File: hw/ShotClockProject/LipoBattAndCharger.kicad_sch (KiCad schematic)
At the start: 28 parts, among them IC1 TP4056-42-ESOP8_Rearanged, J3 SM03B-SRSS-TB(LF)(SN)(P), J4 Conn_01x02_Pin, J5 Conn_01x03_Pin, Q1 Q_PMOS_SGD, Q2 Q_NPN_BCE, Q3 Q_NPN_BCE

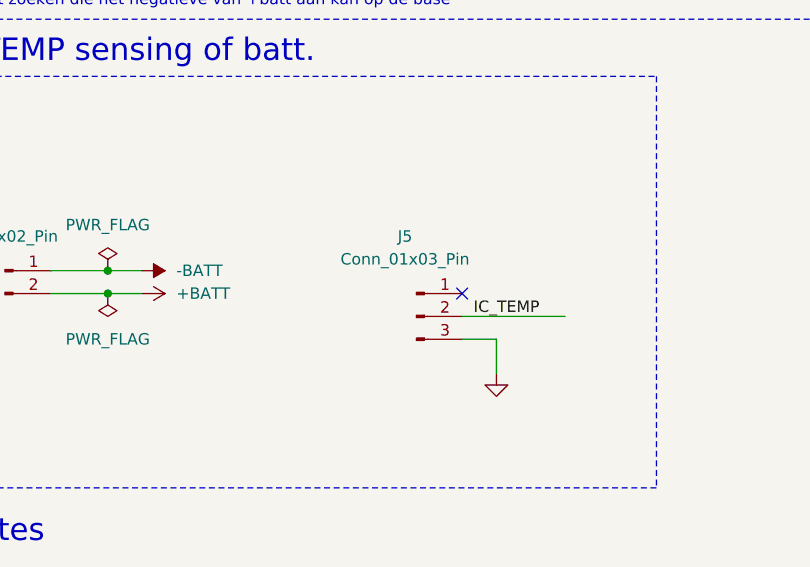
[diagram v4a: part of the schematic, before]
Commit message: Finished mainboard routing
Reconfigered pins to make routing easier/cleaner
Placed copper fills as much as possible to create an even plating index
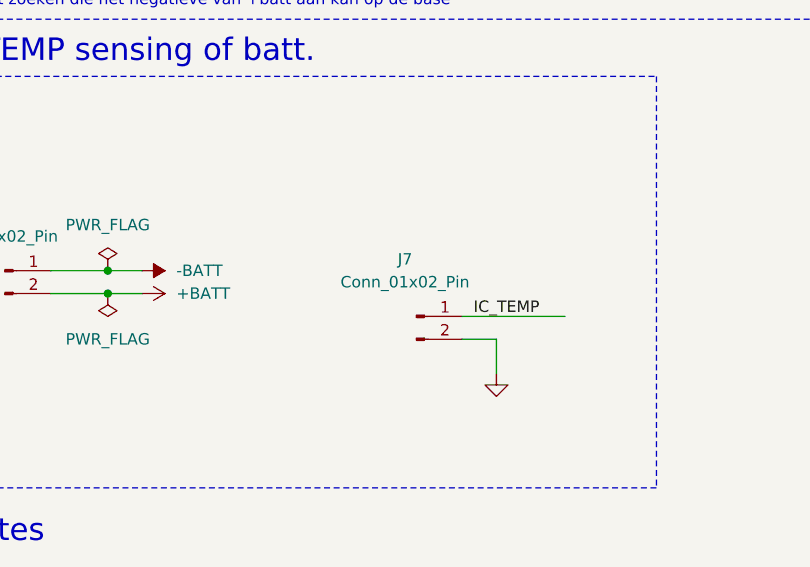
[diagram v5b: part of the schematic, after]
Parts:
- removed J5: Conn_01x03_Pin, Connector_PinHeader_2.54mm:PinHeader_1x03_P2.54mm_Horizontal, symbol Connector:Conn_01x03_Pin
- added J7: Conn_01x02_Pin, Connector_PinHeader_2.54mm:PinHeader_1x02_P2.54mm_Horizontal, symbol Connector:Conn_01x02_Pin
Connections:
- net GND: now also J7.2 (Pin_2)
- net IC_TEMP: now also J7.1 (Pin_1)
- no-connect marks 1 -> 0
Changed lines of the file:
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@@
   (junction (at 50.8 39.37) (diameter 0) (color 0 0 0 0)
   )
+  (junction (at 121.92 55.88) (diameter 0) (color 0 0 0 0)
+  )
+  (junction (at 177.8 49.53) (diameter 0) (color 0 0 0 0)
+  )
+  (junction (at 120.65 113.03) (diameter 0) (color 0 0 0 0)
+  )
+  (junction (at 152.4 67.31) (diameter 0) (color 0 0 0 0)
+  )
   (junction (at 168.91 49.53) (diameter 0) (color 0 0 0 0)
   )
-  (junction (at 121.92 55.88) (diameter 0) (color 0 0 0 0)
-  )
-  (junction (at 177.8 49.53) (diameter 0) (color 0 0 0 0)
-  )
-  (junction (at 120.65 113.03) (diameter 0) (color 0 0 0 0)
-  )
-  (junction (at 152.4 67.31) (diameter 0) (color 0 0 0 0)
-  )
   (junction (at 121.92 69.85) (diameter 0) (color 0 0 0 0)
   )
@@
   (junction (at 233.68 55.88) (diameter 0) (color 0 0 0 0)
   )
-  (no_connect (at 160.02 115.57))
   (wire (pts (xy 66.04 109.22) (xy 66.04 111.76))
     (stroke (width 0) (type default))
@@
     (stroke (width 0) (type default))
   )
+  (wire (pts (xy 152.4 58.42) (xy 152.4 62.23))
+    (stroke (width 0) (type default))
+  )
+  (wire (pts (xy 59.69 39.37) (xy 50.8 39.37))
+    (stroke (width 0) (type default))
+  )
+  (wire (pts (xy 29.21 101.6) (xy 24.765 101.6))
+    (stroke (width 0) (type default))
+  )
+  (wire (pts (xy 179.07 67.31) (xy 177.8 67.31))
+    (stroke (width 0) (type default))
+  )
+  (wire (pts (xy 114.3 113.03) (xy 120.65 113.03))
+    (stroke (width 0) (type default))
+  )
+  (wire (pts (xy 177.8 49.53) (xy 181.61 49.53))
+    (stroke (width 0) (type default))
+  )
+  (wire (pts (xy 41.91 46.99) (xy 41.91 48.26))
+    (stroke (width 0) (type default))
+  )
+  (wire (pts (xy 120.65 113.03) (xy 124.46 113.03))
+    (stroke (width 0) (type default))
+  )
+  (wire (pts (xy 160.02 120.65) (xy 163.83 120.65))
+    (stroke (width 0) (type default))
+  )
+  (wire (pts (xy 233.68 55.88) (xy 233.68 58.42))
+    (stroke (width 0) (type default))
+  )
+  (wire (pts (xy 121.92 55.88) (xy 121.92 57.15))
+    (stroke (width 0) (type default))
+  )
   (wire (pts (xy 135.89 49.53) (xy 168.91 49.53))
-    (stroke (width 0) (type default))
-  )
-  (wire (pts (xy 152.4 58.42) (xy 152.4 62.23))
-    (stroke (width 0) (type default))
-  )
-  (wire (pts (xy 59.69 39.37) (xy 50.8 39.37))
-    (stroke (width 0) (type default))
-  )
-  (wire (pts (xy 29.21 101.6) (xy 24.765 101.6))
-    (stroke (width 0) (type default))
-  )
-  (wire (pts (xy 179.07 67.31) (xy 177.8 67.31))
-    (stroke (width 0) (type default))
-  )
-  (wire (pts (xy 114.3 113.03) (xy 120.65 113.03))
-    (stroke (width 0) (type default))
-  )
-  (wire (pts (xy 177.8 49.53) (xy 181.61 49.53))
-    (stroke (width 0) (type default))
-  )
-  (wire (pts (xy 41.91 46.99) (xy 41.91 48.26))
-    (stroke (width 0) (type default))
-  )
-  (wire (pts (xy 120.65 113.03) (xy 124.46 113.03))
-    (stroke (width 0) (type default))
-  )
-  (wire (pts (xy 160.02 120.65) (xy 163.83 120.65))
-    (stroke (width 0) (type default))
-  )
-  (wire (pts (xy 233.68 55.88) (xy 233.68 58.42))
-    (stroke (width 0) (type default))
-  )
-  (wire (pts (xy 121.92 55.88) (xy 121.92 57.15))
     (stroke (width 0) (type default))
   )
@@
     (effects (font (size 1.27 1.27)) (justify left))
   )
-  (symbol (lib_id "Connector:Conn_01x03_Pin") (at 154.94 118.11 0) (unit 1)
-    (in_bom yes) (on_board yes) (dnp no)
-    (property "Reference" "J5" (at 153.67 109.22 0)
-      (effects (font (size 1.27 1.27)))
-    )
-    (property "Value" "Conn_01x03_Pin" (at 153.67 111.76 0)
-      (effects (font (size 1.27 1.27)))
-    )
-    (property "Footprint" "Connector_PinHeader_2.54mm:PinHeader_1x03_P2.54mm_Horizontal" (at 154.94 118.11 0)
-      (effects (font (size 1.27 1.27)) hide)
-    )
-    (property "Datasheet" "~" (at 154.94 118.11 0)
-      (effects (font (size 1.27 1.27)) hide)
-    )
-    (property "LCSC Part #" "C92159" (at 154.94 118.11 0)
-      (effects (font (size 1.27 1.27)) hide)
-    )
-    (property "LCSC Part" "C92159" (at 154.94 118.11 0)
-      (effects (font (size 1.27 1.27)) hide)
-    )
-    (pin "1")
-    (pin "2")
-    (pin "3")
-    (instances
-      (project "ShotClockProject"
-        (path "/5fd859aa-754d-49c2-9762-3f7ebe3bb64c/d287d155-1951-4d4f-8d6c-570f03bc79f5"
-          (reference "J5") (unit 1)
-        )
-      )
-    )
-  )
   (symbol (lib_id "Device:Q_NPN_BCE") (at 166.37 67.31 0) (unit 1)
     (in_bom yes) (on_board yes) (dnp no)
@@
         )
       )
+    )
+  )
+  (symbol (lib_id "Connector:Conn_01x02_Pin") (at 154.94 118.11 0) (unit 1)
+    (in_bom yes) (on_board yes) (dnp no)
+    (property "Reference" "J7" (at 153.67 111.76 0)
+      (effects (font (size 1.27 1.27)))
+    )
+    (property "Value" "Conn_01x02_Pin" (at 153.67 114.3 0)
+      (effects (font (size 1.27 1.27)))
+    )
+    (property "Footprint" "Connector_PinHeader_2.54mm:PinHeader_1x02_P2.54mm_Horizontal" (at 154.94 118.11 0)
+      (effects (font (size 1.27 1.27)) hide)
+    )
+    (property "Datasheet" "~" (at 154.94 118.11 0)
+      (effects (font (size 1.27 1.27)) hide)
+    )
+    (property "LCSC Part #" "C225269" (at 154.94 118.11 0)
+      (effects (font (size 1.27 1.27)) hide)
+    )
+    (property "LCSC Part" "C225269" (at 154.94 118.11 0)
+      (effects (font (size 1.27 1.27)) hide)
+    )
+    (pin "1")
+    (pin "2")
+    (instances
+      (project "ShotClockProject"
+        (path "/5fd859aa-754d-49c2-9762-3f7ebe3bb64c/d287d155-1951-4d4f-8d6c-570f03bc79f5"
+          (reference "J7") (unit 1)
+        )
+      )

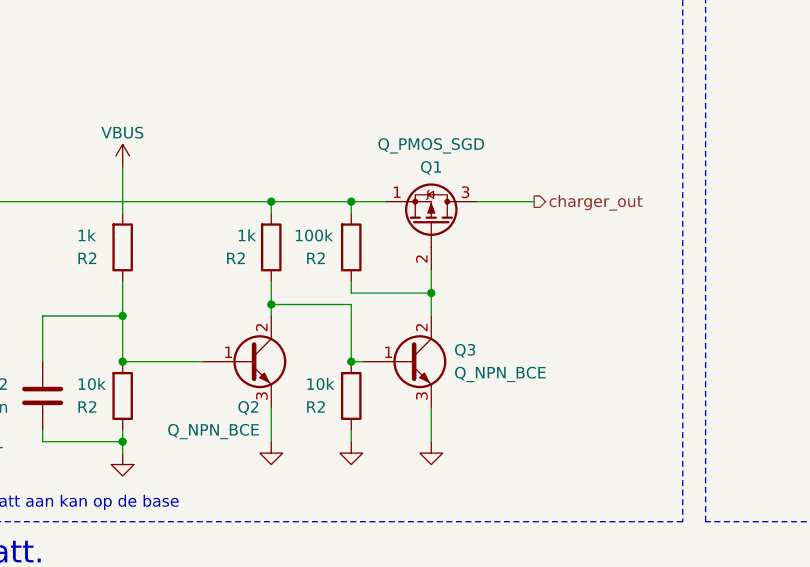
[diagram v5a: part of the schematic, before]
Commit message: Finished routing and added silk + part nmbr
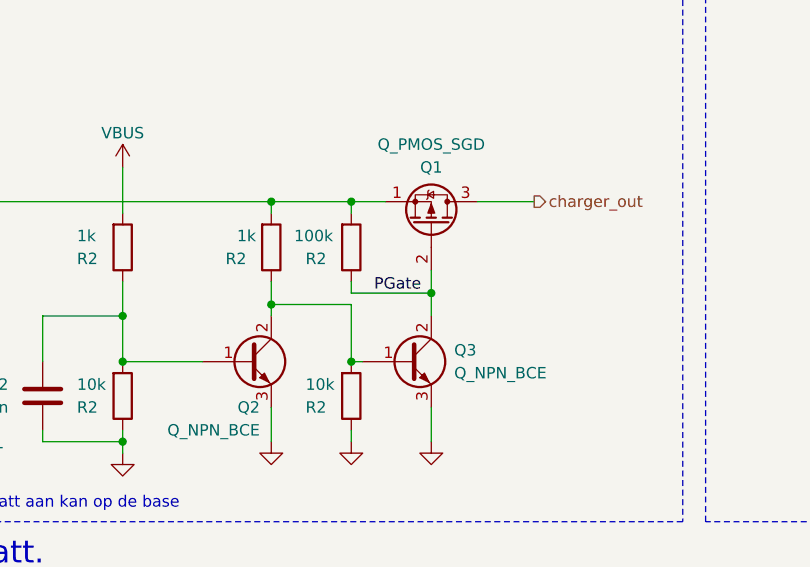
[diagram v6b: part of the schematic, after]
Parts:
- C12, C13: LCSC Part # C96446 -> (none)
- C12: LCSC Part C57112 -> C15195; LCSC Part # C57112 -> (none)
- C12: LCSC Part # C1525 -> (none)
- D1: LCSC Part # C128250 -> (none)
- D2: LCSC Part # C72043 -> (none)
- IC1: LCSC Part # C725790 -> (none)
- J3: LCSC Part # C160403 -> (none)
- J4, J7: LCSC Part # C225269 -> (none)
- Q1: LCSC Part # C33903 -> (none)
- Q2, Q3: LCSC Part # C111113 -> (none)
- R11, R17: LCSC Part C144787 -> C25741; LCSC Part # C144787 -> (none)
- R2, R5, R6: LCSC Part # C105637 -> (none)
- R2: LCSC Part # C25744 -> (none)
- R2: LCSC Part # C25741 -> (none)
- R3: LCSC Part # C27147 -> (none)
- R4: LCSC Part # C852935 -> (none)
- R4: LCSC Part # C25862 -> (none)
- R4: LCSC Part # C25900 -> (none)
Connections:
- net PGate: now reaches Q1.2 (G), Q3.2 (C), R2.1
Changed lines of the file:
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@@
+    (effects (font (size 1.27 1.27)) (justify left bottom))
+  )
+  (label "PGate" (at 180.34 59.69 0) (fields_autoplaced)
     (effects (font (size 1.27 1.27)) (justify left bottom))
   )
@@
       (effects (font (size 1.27 1.27)) hide)
     )
-    (property "LCSC Part #" "C111113" (at 166.37 67.31 0)
+    (property "LCSC Part #" "" (at 166.37 67.31 0)
       (effects (font (size 1.27 1.27)) hide)
     )
@@
       (effects (font (size 1.27 1.27)) hide)
     )
-    (property "LCSC Part #" "C105637" (at 41.91 52.07 0)
+    (property "LCSC Part #" "" (at 41.91 52.07 0)
       (effects (font (size 1.27 1.27)) hide)
     )
@@
       (effects (font (size 1.27 1.27)) hide)
     )
-    (property "LCSC Part #" "C105637" (at 152.4 54.61 0)
+    (property "LCSC Part #" "" (at 152.4 54.61 0)
       (effects (font (size 1.27 1.27)) hide)
     )
@@
       (effects (font (size 1.27 1.27)) hide)
     )
-    (property "LCSC Part #" "C25744" (at 177.8 71.12 0)
+    (property "LCSC Part #" "" (at 177.8 71.12 0)
       (effects (font (size 1.27 1.27)) hide)
     )
@@
       (effects (font (size 1.27 1.27)) hide)
     )
-    (property "LCSC Part #" "C160403" (at 34.29 111.76 0)
+    (property "LCSC Part #" "" (at 34.29 111.76 0)
       (effects (font (size 1.27 1.27)) hide)
     )
@@
       (effects (font (size 1.27 1.27)) hide)
     )
-    (property "LCSC Part #" "C33903" (at 186.69 52.07 0)
+    (property "LCSC Part #" "" (at 186.69 52.07 0)
       (effects (font (size 1.27 1.27)) hide)
     )
@@
       (effects (font (size 1.27 1.27)) hide)
     )
-    (property "LCSC Part #" "C72043" (at 41.91 43.18 0)
+    (property "LCSC Part #" "" (at 41.91 43.18 0)
       (effects (font (size 1.27 1.27)) hide)
     )
@@
       (effects (font (size 1.27 1.27)) hide)
     )
-    (property "LCSC Part #" "C225269" (at 109.22 113.03 0)
+    (property "LCSC Part #" "" (at 109.22 113.03 0)
       (effects (font (size 1.27 1.27)) hide)
     )
@@
       (effects (font (size 1.27 1.27)) hide)
     )
-    (property "LCSC Part #" "C96446" (at 121.92 60.96 0)
+    (property "LCSC Part #" "" (at 121.92 60.96 0)
       (effects (font (size 1.27 1.27)) hide)
     )
@@
       (effects (font (size 1.27 1.27)) hide)
     )
-    (property "LCSC Part #" "C225269" (at 154.94 118.11 0)
+    (property "LCSC Part #" "" (at 154.94 118.11 0)
       (effects (font (size 1.27 1.27)) hide)
     )
@@
       (effects (font (size 1.27 1.27)) hide)
     )
-    (property "LCSC Part #" "C852935" (at 66.04 119.38 0)
+    (property "LCSC Part #" "" (at 66.04 119.38 0)
       (effects (font (size 1.27 1.27)) hide)
     )
@@
       (effects (font (size 1.27 1.27)) hide)
     )
-    (property "LCSC Part #" "C27147" (at 59.69 35.56 0)
+    (property "LCSC Part #" "" (at 59.69 35.56 0)
       (effects (font (size 1.27 1.27)) hide)
     )
@@
       (effects (font (size 1.27 1.27)) hide)
     )
-    (property "LCSC Part #" "C57112" (at 143.51 71.12 0)
-      (effects (font (size 1.27 1.27)) hide)
-    )
-    (property "LCSC Part" "C57112" (at 143.51 71.12 0)
+    (property "LCSC Part #" "" (at 143.51 71.12 0)
+      (effects (font (size 1.27 1.27)) hide)
+    )
+    (property "LCSC Part" "C15195" (at 143.51 71.12 0)
       (effects (font (size 1.27 1.27)) hide)
     )
@@
       (effects (font (size 1.27 1.27)) hide)
     )
-    (property "LCSC Part #" "C25862" (at 114.3 66.04 0)
+    (property "LCSC Part #" "" (at 114.3 66.04 0)
       (effects (font (size 1.27 1.27)) hide)
     )
@@
       (effects (font (size 1.27 1.27)) hide)
     )
-    (property "LCSC Part #" "C25741" (at 177.8 54.61 0)
+    (property "LCSC Part #" "" (at 177.8 54.61 0)
       (effects (font (size 1.27 1.27)) hide)
     )
@@
       (effects (font (size 1.27 1.27)) hide)
     )
-    (property "LCSC Part #" "C25900" (at 66.04 105.41 0)
+    (property "LCSC Part #" "" (at 66.04 105.41 0)
       (effects (font (size 1.27 1.27)) hide)
     )
@@
       (effects (font (size 1.27 1.27)) hide)
     )
-    (property "LCSC Part #" "C128250" (at 50.8 43.18 0)
+    (property "LCSC Part #" "" (at 50.8 43.18 0)
       (effects (font (size 1.27 1.27)) hide)
     )
@@
       (effects (font (size 1.27 1.27)) (justify left top) hide)
     )
-    (property "LCSC Part #" "C725790" (at 97.79 55.88 0)
+    (property "LCSC Part #" "" (at 97.79 55.88 0)
       (effects (font (size 1.27 1.27)) hide)
     )
@@
       (effects (font (size 1.27 1.27)) hide)
     )
-    (property "LCSC Part #" "C144787" (at 233.68 49.53 0)
-      (effects (font (size 1.27 1.27)) hide)
-    )
-    (property "LCSC Part" "C144787" (at 233.68 49.53 0)
+    (property "LCSC Part #" "" (at 233.68 49.53 0)
+      (effects (font (size 1.27 1.27)) hide)
+    )
+    (property "LCSC Part" "C25741" (at 233.68 49.53 0)
       (effects (font (size 1.27 1.27)) hide)
     )
@@
       (effects (font (size 1.27 1.27)) hide)
     )
-    (property "LCSC Part #" "C96446" (at 31.75 44.45 0)
+    (property "LCSC Part #" "" (at 31.75 44.45 0)
       (effects (font (size 1.27 1.27)) hide)
     )
@@
       (effects (font (size 1.27 1.27)) hide)
     )
-    (property "LCSC Part #" "C105637" (at 168.91 54.61 0)
+    (property "LCSC Part #" "" (at 168.91 54.61 0)
       (effects (font (size 1.27 1.27)) hide)
     )
@@
       (effects (font (size 1.27 1.27)) hide)
     )
-    (property "LCSC Part #" "C111113" (at 184.15 67.31 0)
+    (property "LCSC Part #" "" (at 184.15 67.31 0)
       (effects (font (size 1.27 1.27)) hide)
     )
@@
       (effects (font (size 1.27 1.27)) hide)
     )
-    (property "LCSC Part #" "C105637" (at 50.8 52.07 0)
+    (property "LCSC Part #" "" (at 50.8 52.07 0)
       (effects (font (size 1.27 1.27)) hide)
     )
@@
       (effects (font (size 1.27 1.27)) hide)
     )
-    (property "LCSC Part #" "C1525" (at 243.84 62.23 0)
+    (property "LCSC Part #" "" (at 243.84 62.23 0)
       (effects (font (size 1.27 1.27)) hide)
     )
@@
       (effects (font (size 1.27 1.27)) hide)
     )
-    (property "LCSC Part #" "C25744" (at 152.4 71.12 0)
+    (property "LCSC Part #" "" (at 152.4 71.12 0)
       (effects (font (size 1.27 1.27)) hide)
     )
@@
       (effects (font (size 1.27 1.27)) hide)
     )
-    (property "LCSC Part #" "C144787" (at 233.68 62.23 0)
-      (effects (font (size 1.27 1.27)) hide)
-    )
-    (property "LCSC Part" "C144787" (at 233.68 62.23 0)
-      (effects (font (size 1.27 1.27)) hide)
-    )
+    (property "LCSC Part #" "" (at 233.68 62.23 0)
+      (effects (font (size 1.27 1.27)) hide)
+    )
+    (property "LCSC Part" "C25741" (at 233.68 62.23 0)
+      (effects (font (size 1.27 1.27)) hide)
+    )

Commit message: Fixed mainboard with feedback from Luc
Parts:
- removed TP4: TestPoint, TestPoint:TestPoint_Pad_D1.0mm, symbol Connector:TestPoint
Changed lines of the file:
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@@
-    )
-  )
-  (symbol (lib_id "Connector:TestPoint") (at 243.84 55.88 0) (unit 1)
-    (in_bom yes) (on_board yes) (dnp no)
-    (property "Reference" "TP4" (at 242.57 48.26 0)
-      (effects (font (size 1.27 1.27)) (justify left))
-    )
-    (property "Value" "TestPoint" (at 242.57 50.8 0)
-      (effects (font (size 1.27 1.27)) (justify left))
-    )
-    (property "Footprint" "TestPoint:TestPoint_Pad_D1.0mm" (at 248.92 55.88 0)
-      (effects (font (size 1.27 1.27)) hide)
-    )
-    (property "Datasheet" "~" (at 248.92 55.88 0)
-      (effects (font (size 1.27 1.27)) hide)
-    )
-    (property "LCSC Part #" "" (at 243.84 55.88 0)
-      (effects (font (size 1.27 1.27)) hide)
-    )
-    (property "LCSC Part" "" (at 243.84 55.88 0)
-      (effects (font (size 1.27 1.27)) hide)
-    )
-    (pin "1")
-    (instances
-      (project "ShotClockProject"
-        (path "/5fd859aa-754d-49c2-9762-3f7ebe3bb64c"
-          (reference "TP4") (unit 1)
-        )
-        (path "/5fd859aa-754d-49c2-9762-3f7ebe3bb64c/dbe9281d-d28a-4966-832c-4ef9ca7a9777"
-          (reference "TP13") (unit 1)
-        )
-        (path "/5fd859aa-754d-49c2-9762-3f7ebe3bb64c/d287d155-1951-4d4f-8d6c-570f03bc79f5"
-          (reference "TP9") (unit 1)
-        )
-      )
     )
   )
